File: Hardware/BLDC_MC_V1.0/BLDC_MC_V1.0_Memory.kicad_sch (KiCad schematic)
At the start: 9 parts, among them U3 25LC256-E_SN

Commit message: add the new edits to Buck converter sheet and edit other sheets name
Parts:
- C17: footprint Capacitor_SMD:C_0603_1608Metric -> Capacitor_SMD:C_0805_2012Metric; LCSC_PN C1591 -> C28233; MP CL10B104KB8NNNC -> CL21B104KCFNNNE
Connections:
- net +3.3V: now also C17.1; no longer C17.2
- net GND: now also C17.2; no longer C17.1

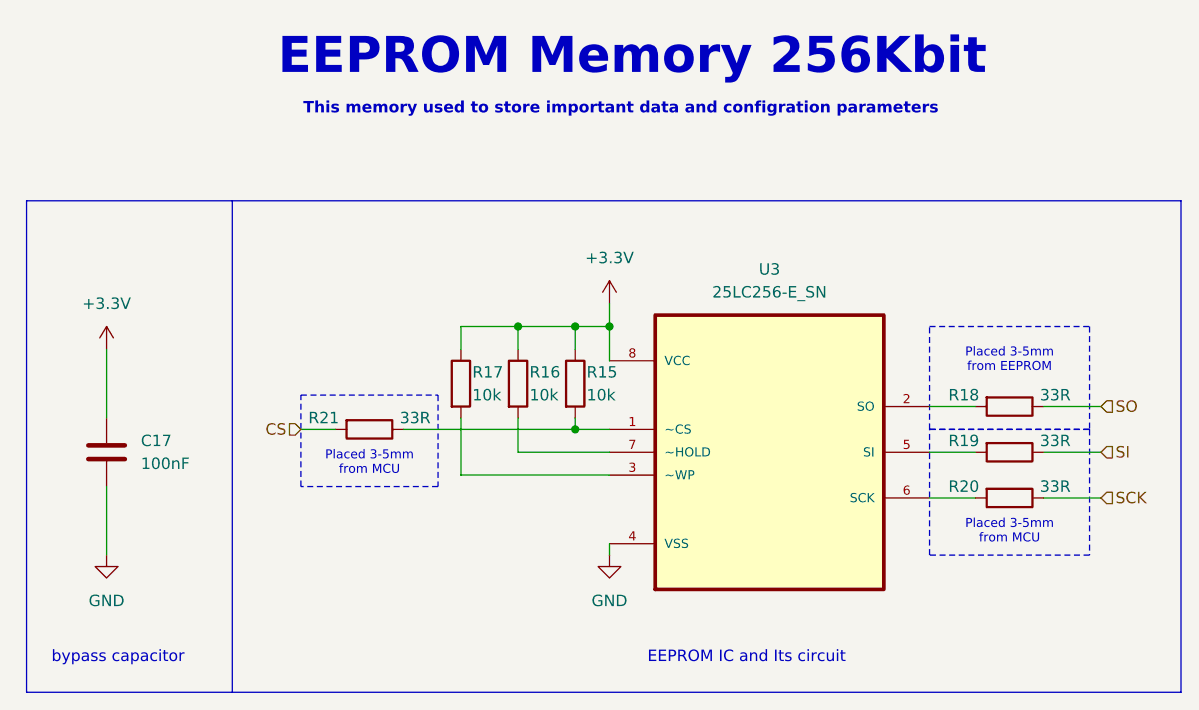
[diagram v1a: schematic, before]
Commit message: Edit the connection between sheets and add some details and connections to gatedrive sheet
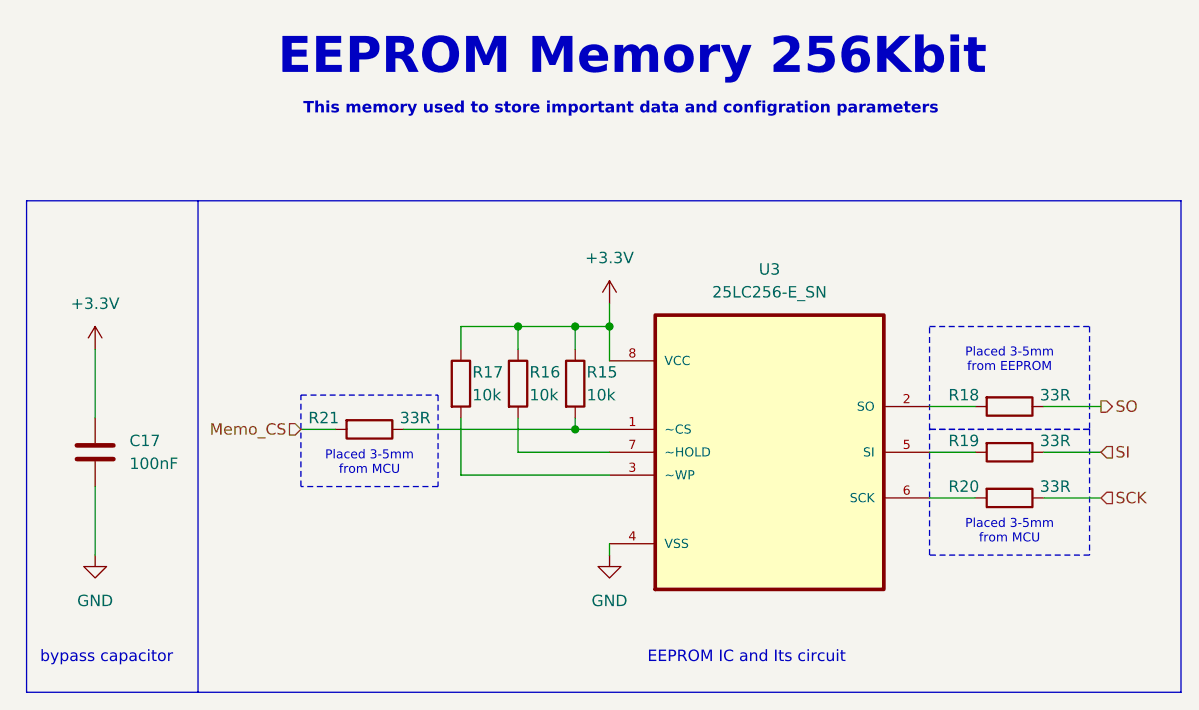
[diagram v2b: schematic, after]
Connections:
- net CS renamed Memo_CS
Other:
- moved on the sheet: C17
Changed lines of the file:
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@@
 	(text "bypass capacitor\n"
 		(exclude_from_sim no)
-		(at 90.17 120.65 0)
+		(at 88.9 120.65 0)
 		(effects
 			(font
@@
 	(wire
 		(pts
-			(xy 88.9 101.6) (xy 88.9 109.22)
+			(xy 87.63 101.6) (xy 87.63 109.22)
 		)
 		(stroke
@@
 	(wire
 		(pts
-			(xy 88.9 86.36) (xy 88.9 93.98)
+			(xy 87.63 86.36) (xy 87.63 93.98)
 		)
 		(stroke
@@
 	(polyline
 		(pts
-			(xy 102.87 69.85) (xy 102.87 124.46)
+			(xy 99.06 69.85) (xy 99.06 124.46)
 		)
 		(stroke
@@
 	)
 	(hierarchical_label "SO"
-		(shape input)
+		(shape output)
 		(at 199.39 92.71 0)
 		(effects
@@
 		)
 	)
-	(hierarchical_label "CS"
+	(hierarchical_label "Memo_CS"
 		(shape input)
 		(at 110.49 95.25 180)
@@
 	(symbol
 		(lib_id "power:GND")
-		(at 88.9 109.22 0)
+		(at 87.63 109.22 0)
 		(unit 1)
 		(exclude_from_sim no)
@@
 		(fields_autoplaced yes)
 		(property "Reference" "#PWR031"
-			(at 88.9 115.57 0)
+			(at 87.63 115.57 0)
 			(effects
 				(font
@@
 		)
 		(property "Value" "GND"
-			(at 88.9 114.3 0)
+			(at 87.63 114.3 0)
 			(effects
 				(font
@@
 		)
 		(property "Footprint" ""
-			(at 88.9 109.22 0)
+			(at 87.63 109.22 0)
 			(effects
 				(font
@@
 		)
 		(property "Datasheet" ""
-			(at 88.9 109.22 0)
+			(at 87.63 109.22 0)
 			(effects
 				(font
@@
 		)
 		(property "Description" "Power symbol creates a global label with name \"GND\" , ground"
-			(at 88.9 109.22 0)
+			(at 87.63 109.22 0)
 			(effects
 				(font
@@
 	(symbol
 		(lib_id "Device:C")
-		(at 88.9 97.79 0)
+		(at 87.63 97.79 0)
 		(unit 1)
 		(exclude_from_sim no)
@@
 		(fields_autoplaced yes)
 		(property "Reference" "C17"
-			(at 92.71 96.5199 0)
+			(at 91.44 96.5199 0)
 			(effects
 				(font
@@
 		)
 		(property "Value" "100nF"
-			(at 92.71 99.0599 0)
+			(at 91.44 99.0599 0)
 			(effects
 				(font
@@
 		)
 		(property "Footprint" "Capacitor_SMD:C_0805_2012Metric"
-			(at 89.8652 101.6 0)
+			(at 88.5952 101.6 0)
 			(effects
 				(font
@@
 		)
 		(property "Datasheet" "https://www.lcsc.com/datasheet/C28233.pdf"
-			(at 88.9 97.79 0)
+			(at 87.63 97.79 0)
 			(effects
 				(font
@@
 		)
 		(property "Description" "Unpolarized capacitor"
-			(at 88.9 97.79 0)
+			(at 87.63 97.79 0)
 			(effects
 				(font
@@
 		)
 		(property "LCSC_PN" "C28233"
-			(at 88.9 97.79 0)
+			(at 87.63 97.79 0)
 			(effects
 				(font
@@
 		)
 		(property "MP" "CL21B104KCFNNNE"
-			(at 88.9 97.79 0)
+			(at 87.63 97.79 0)
 			(effects
 				(font
@@
 		)
 		(property "Assembled" "Yes"
-			(at 88.9 97.79 0)
+			(at 87.63 97.79 0)
 			(effects
 				(font
@@
 	(symbol
 		(lib_id "power:+3.3V")
-		(at 88.9 86.36 0)
+		(at 87.63 86.36 0)
 		(unit 1)
 		(exclude_from_sim no)
@@
 		(fields_autoplaced yes)
 		(property "Reference" "#PWR032"
-			(at 88.9 90.17 0)
+			(at 87.63 90.17 0)
 			(effects
 				(font
@@
 		)
 		(property "Value" "+3.3V"
-			(at 88.9 81.28 0)
+			(at 87.63 81.28 0)
 			(effects
 				(font
@@
 		)
 		(property "Footprint" ""
-			(at 88.9 86.36 0)
+			(at 87.63 86.36 0)
 			(effects
 				(font
@@
 		)
 		(property "Datasheet" ""
-			(at 88.9 86.36 0)
+			(at 87.63 86.36 0)
 			(effects
 				(font
@@
 		)
 		(property "Description" "Power symbol creates a global label with name \"+3.3V\""
-			(at 88.9 86.36 0)
-			(effects
-				(font
+			(at 87.63 86.36 0)
+			(effects
+				(font

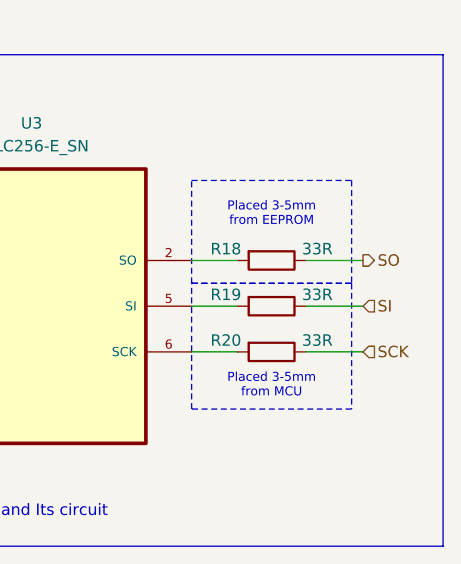
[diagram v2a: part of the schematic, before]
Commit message: Edit Controller sheet and add oscillators for the controller
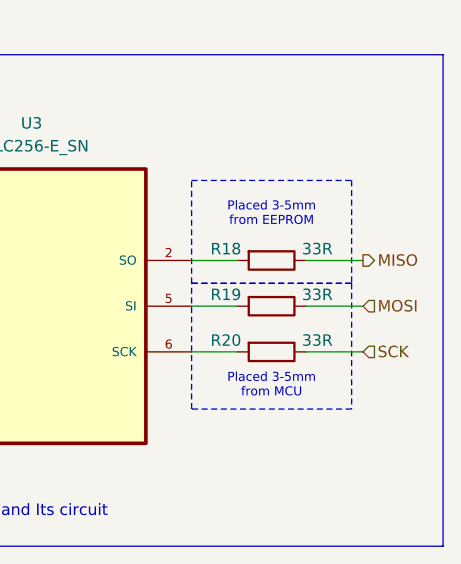
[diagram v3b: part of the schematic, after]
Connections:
- net SI renamed MOSI
- net SO renamed MISO
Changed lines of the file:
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@@
 		)
 	)
-	(hierarchical_label "SI"
+	(hierarchical_label "MOSI"
 		(shape input)
 		(at 199.39 97.79 0)
@@
 		)
 	)
-	(hierarchical_label "SO"
+	(hierarchical_label "MISO"
 		(shape output)
 		(at 199.39 92.71 0)

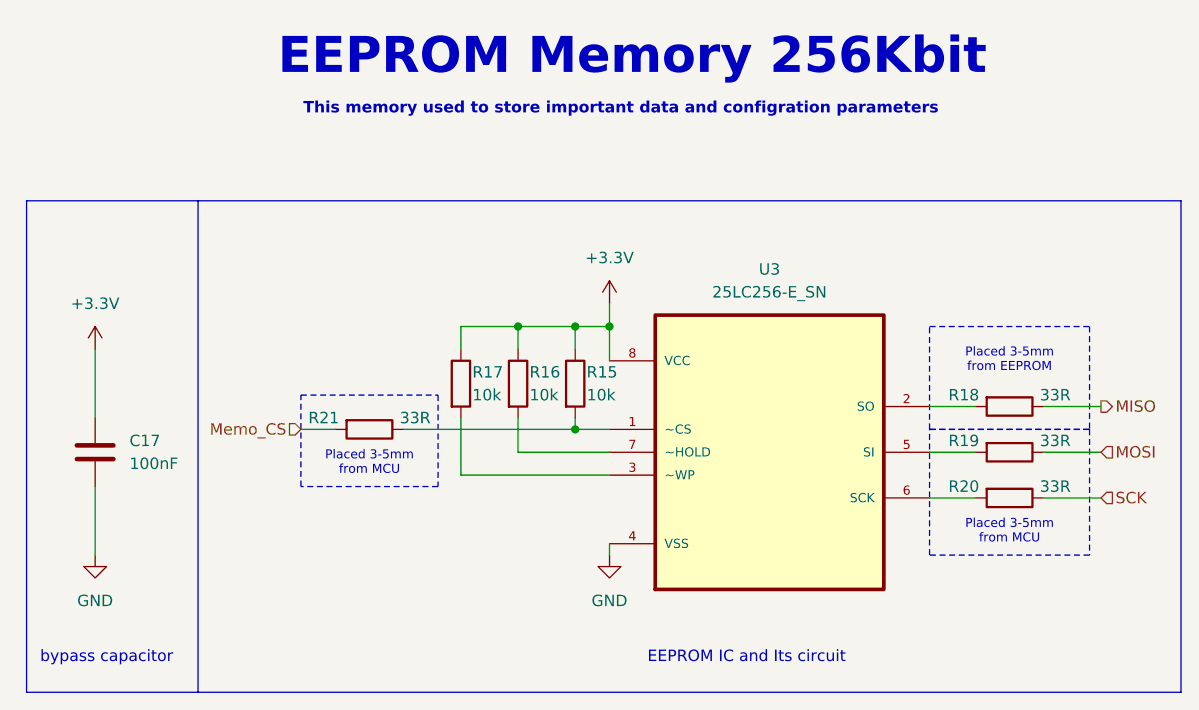
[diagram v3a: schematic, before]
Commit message: Add hall sensor sheet and its simulation file
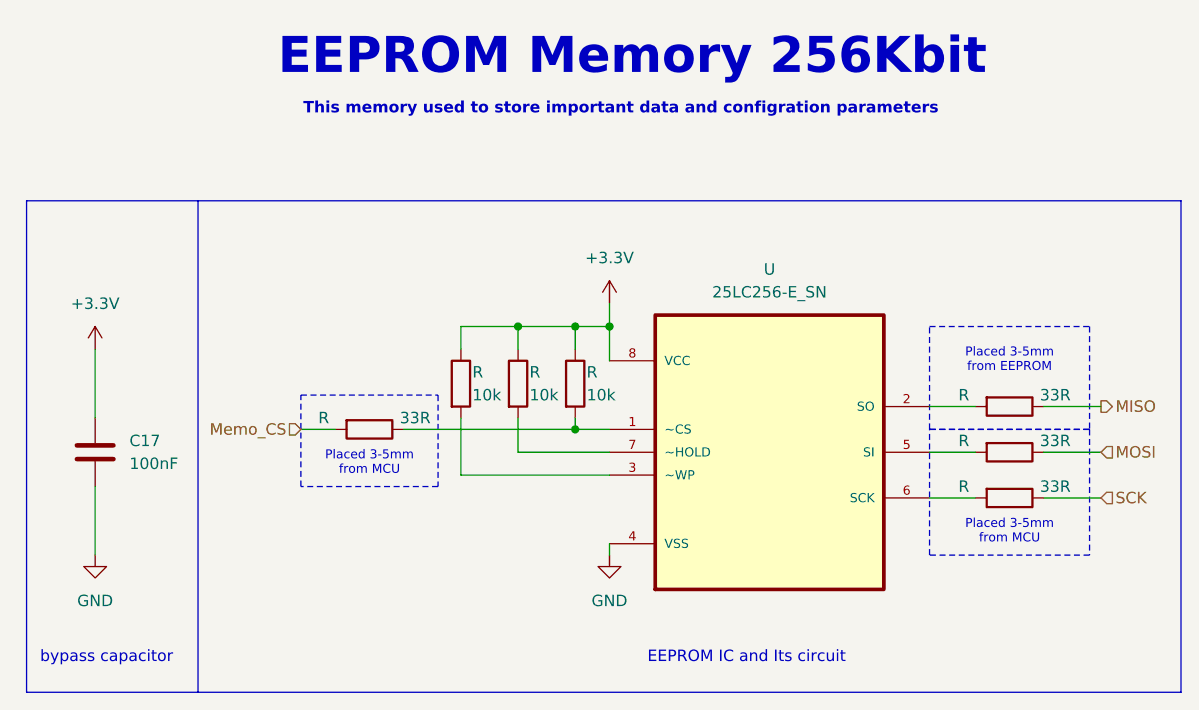
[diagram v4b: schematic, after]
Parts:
- renumbered R20 to R, R19 to R, R17 to R, R21 to R, R16 to R, R18 to R, R15 to R, U3 to U
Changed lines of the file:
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@@
 		(dnp no)
 		(fields_autoplaced yes)
-		(property "Reference" "#PWR030"
+		(property "Reference" "#PWR"
 			(at 144.78 115.57 0)
 			(effects
@@
 		(pin "1"
 		)
-		(instances
-			(project ""
-				(path "/e34fda66-7244-4ac9-bbf7-3725f03e688f/bcfa60d7-9b39-4a60-8e0a-1c9d768132f8"
-					(reference "#PWR030")
-					(unit 1)
-				)
-			)
-		)
+		(instances)
 	)
 	(symbol
@@
 		(on_board yes)
 		(dnp no)
-		(property "Reference" "R20"
+		(property "Reference" "R"
 			(at 184.15 101.6 90)
 			(effects
@@
 		(pin "1"
 		)
-		(instances
-			(project "BLDC_Motor_Driver"
-				(path "/e34fda66-7244-4ac9-bbf7-3725f03e688f/bcfa60d7-9b39-4a60-8e0a-1c9d768132f8"
-					(reference "R20")
-					(unit 1)
-				)
-			)
-		)
+		(instances)
 	)
 	(symbol
@@
 		(on_board yes)
 		(dnp no)
-		(property "Reference" "R19"
+		(property "Reference" "R"
 			(at 184.15 96.52 90)
 			(effects
@@
 		(pin "1"
 		)
-		(instances
-			(project "BLDC_Motor_Driver"
-				(path "/e34fda66-7244-4ac9-bbf7-3725f03e688f/bcfa60d7-9b39-4a60-8e0a-1c9d768132f8"
-					(reference "R19")
-					(unit 1)
-				)
-			)
-		)
+		(instances)
 	)
 	(symbol
@@
 		(on_board yes)
 		(dnp no)
-		(property "Reference" "R17"
+		(property "Reference" "R"
 			(at 129.54 88.9 0)
 			(effects
@@
 		(pin "2"
 		)
-		(instances
-			(project "BLDC_Motor_Driver"
-				(path "/e34fda66-7244-4ac9-bbf7-3725f03e688f/bcfa60d7-9b39-4a60-8e0a-1c9d768132f8"
-					(reference "R17")
-					(unit 1)
-				)
-			)
-		)
+		(instances)
 	)
 	(symbol
@@
 		(on_board yes)
 		(dnp no)
-		(property "Reference" "R21"
+		(property "Reference" "R"
 			(at 113.03 93.98 90)
 			(effects
@@
 		(pin "1"
 		)
-		(instances
-			(project "BLDC_Motor_Driver"
-				(path "/e34fda66-7244-4ac9-bbf7-3725f03e688f/bcfa60d7-9b39-4a60-8e0a-1c9d768132f8"
-					(reference "R21")
-					(unit 1)
-				)
-			)
-		)
+		(instances)
 	)
 	(symbol
@@
 		(dnp no)
 		(fields_autoplaced yes)
-		(property "Reference" "#PWR031"
+		(property "Reference" "#PWR"
 			(at 87.63 115.57 0)
 			(effects
@@
 		(pin "1"
 		)
-		(instances
-			(project "BLDC_Motor_Driver"
-				(path "/e34fda66-7244-4ac9-bbf7-3725f03e688f/bcfa60d7-9b39-4a60-8e0a-1c9d768132f8"
-					(reference "#PWR031")
-					(unit 1)
-				)
-			)
-		)
+		(instances)
 	)
 	(symbol
@@
 		(on_board yes)
 		(dnp no)
-		(property "Reference" "R16"
+		(property "Reference" "R"
 			(at 135.89 88.9 0)
 			(effects
@@
 		(pin "2"
 		)
-		(instances
-			(project "BLDC_Motor_Driver"
-				(path "/e34fda66-7244-4ac9-bbf7-3725f03e688f/bcfa60d7-9b39-4a60-8e0a-1c9d768132f8"
-					(reference "R16")
-					(unit 1)
-				)
-			)
-		)
+		(instances)
 	)
 	(symbol
@@
 		(on_board yes)
 		(dnp no)
-		(property "Reference" "R18"
+		(property "Reference" "R"
 			(at 184.15 91.44 90)
 			(effects
@@
 		(pin "1"
 		)
-		(instances
-			(project ""
-				(path "/e34fda66-7244-4ac9-bbf7-3725f03e688f/bcfa60d7-9b39-4a60-8e0a-1c9d768132f8"
-					(reference "R18")
-					(unit 1)
-				)
-			)
-		)
+		(instances)
 	)
 	(symbol
@@
 		(dnp no)
 		(fields_autoplaced yes)
-		(property "Reference" "#PWR032"
+		(property "Reference" "#PWR"
 			(at 87.63 90.17 0)
 			(effects
@@
 		(pin "1"
 		)
-		(instances
-			(project "BLDC_Motor_Driver"
-				(path "/e34fda66-7244-4ac9-bbf7-3725f03e688f/bcfa60d7-9b39-4a60-8e0a-1c9d768132f8"
-					(reference "#PWR032")
-					(unit 1)
-				)
-			)
-		)
+		(instances)
 	)
 	(symbol
@@
 		(on_board yes)
 		(dnp no)
-		(property "Reference" "R15"
+		(property "Reference" "R"
 			(at 142.24 88.9 0)
 			(effects
@@
 		(pin "2"
 		)
-		(instances
-			(project ""
-				(path "/e34fda66-7244-4ac9-bbf7-3725f03e688f/bcfa60d7-9b39-4a60-8e0a-1c9d768132f8"
-					(reference "R15")
-					(unit 1)
-				)
-			)
-		)
+		(instances)
 	)
 	(symbol
@@
 		(dnp no)
 		(fields_autoplaced yes)
-		(property "Reference" "U3"
+		(property "Reference" "U"
 			(at 162.56 77.47 0)
 			(effects
@@
 		(pin "1"
 		)
-		(instances
-			(project ""
-				(path "/e34fda66-7244-4ac9-bbf7-3725f03e688f/bcfa60d7-9b39-4a60-8e0a-1c9d768132f8"
-					(reference "U3")
-					(unit 1)
-				)
-			)
-		)
+		(instances)
 	)
 	(symbol
@@
 		(dnp no)
 		(fields_autoplaced yes)
-		(property "Reference" "#PWR029"
+		(property "Reference" "#PWR"
 			(at 144.78 85.09 0)
 			(effects
@@
 		(pin "1"
 		)
-		(instances
-			(project ""
-				(path "/e34fda66-7244-4ac9-bbf7-3725f03e688f/bcfa60d7-9b39-4a60-8e0a-1c9d768132f8"
-					(reference "#PWR029")
-					(unit 1)
-				)
-			)
-		)
+		(instances)
 	)
 )
